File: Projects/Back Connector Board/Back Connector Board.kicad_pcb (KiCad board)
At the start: 2 copper layers, 12 parts, among them J1 Conn_02x09_Odd_Even, J10 Molex_MiniFit_02x04, J11 Molex_MiniFit_02x04, J12 Molex_MiniFit_02x04, J2 Conn_02x09_Odd_Even, J3 Conn_02x09_Odd_Even, J4 Conn_02x09_Odd_Even, J5 Conn_02x08_Odd_Even, J6 Conn_02x08_Odd_Even, J7 Molex_MiniFit_02x04, J8 Molex_MiniFit_02x04, J9 Molex_MiniFit_02x04

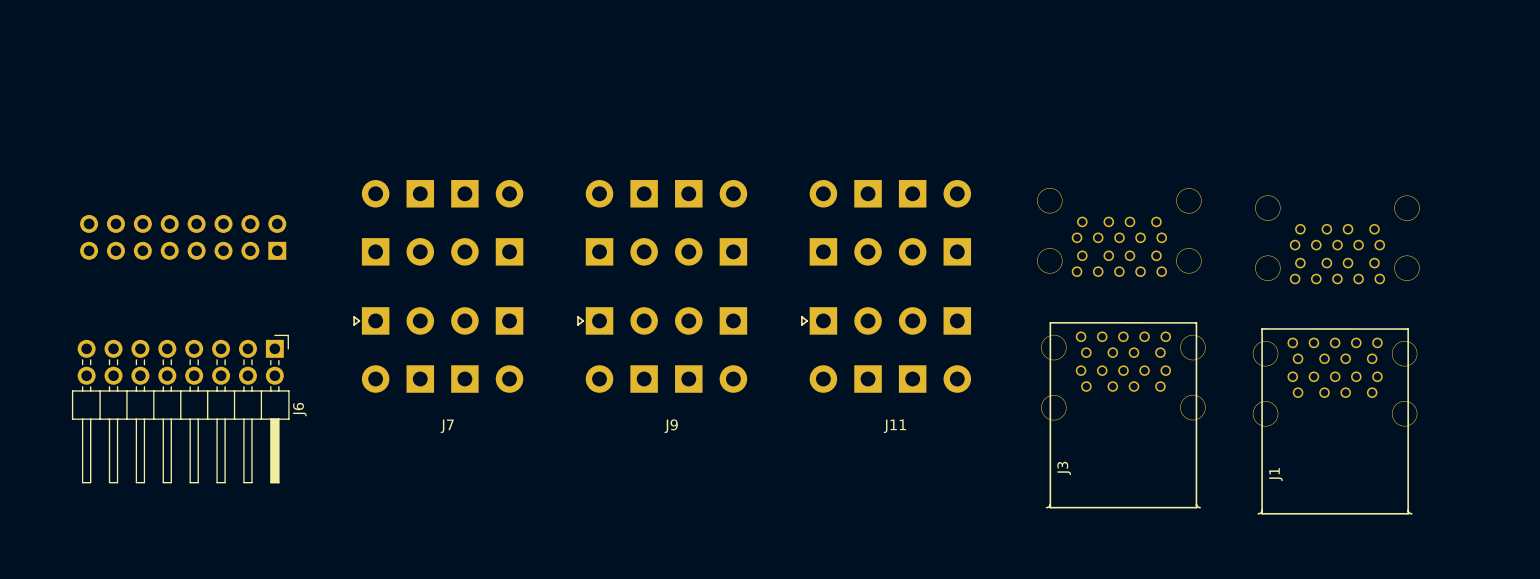
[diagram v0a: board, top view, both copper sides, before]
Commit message: Almost finished Back Connector Board; Just need to consult mechs
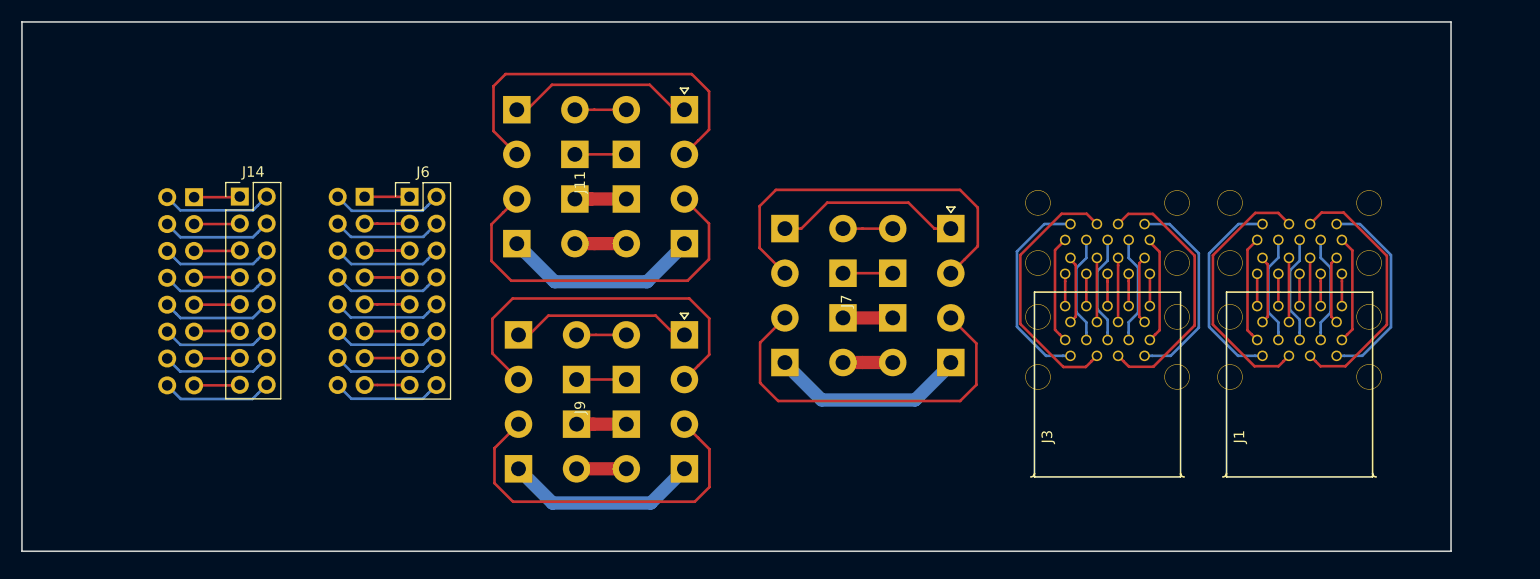
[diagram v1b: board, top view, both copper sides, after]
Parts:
- added J13: Conn_02x08_Odd_Even, Pin_Headers:Pin_Header_Straight_2x08_Pitch2.54mm, B.Cu at (107.5, 60.8)
- added J14: Conn_02x08_Odd_Even, Pin_Headers:Pin_Header_Straight_2x08_Pitch2.54mm, F.Cu at (111.9, 60.7)
- J5, J6: footprint Pin_Headers:Pin_Header_Angled_2x08_Pitch2.54mm -> Pin_Headers:Pin_Header_Straight_2x08_Pitch2.54mm
- moved J8 45.7 mm to (174.5, 70.6), turned to 270 degrees
- moved J11 39.4 mm to (142.7, 59.4), turned to 270 degrees
- moved J7 38.6 mm to (167.9, 70.6), turned to 270 degrees
- moved J10 26.0 mm to (149.3, 80.6), turned to 270 degrees
- moved J12 25.1 mm to (149.2, 59.4), turned to 270 degrees
- moved J6 19.2 mm to (127.9, 60.7), turned to 0 degrees
- moved J9 10.4 mm to (142.7, 80.6), turned to 270 degrees
- moved J5 9.70 mm to (123.6, 60.7), turned to 180 degrees
- moved J1 4.84 mm to (211.4, 73.3)
- moved J2 3.61 mm to (211.4, 65.8)
- moved J3 3.26 mm to (193.3, 73.3)
- moved J4 1.14 mm to (193.3, 65.8)
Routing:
- net Net-(J7-Pad2): track 0.00 -> 36.5 mm
- net Net-(J7-Pad3): track 0.00 -> 36.2 mm
- net Net-(J11-Pad2): track 0.00 -> 35.8 mm
- net Net-(J11-Pad3): track 0.00 -> 35.7 mm
- net Net-(J10-Pad2): track 0.00 -> 35.6 mm
- net Net-(J10-Pad3): track 0.00 -> 35.0 mm
- net Net-(J1-Pad3): track 0.00 -> 25.2 mm
- net Net-(J3-Pad3): track 0.00 -> 25.1 mm
- net Net-(J3-Pad2): track 0.00 -> 25.1 mm
- net Net-(J1-Pad2): track 0.00 -> 25.1 mm
- net Net-(J3-Pad4): track 0.00 -> 19.5 mm
- net Net-(J3-Pad1): track 0.00 -> 19.4 mm
- net Net-(J1-Pad4): track 0.00 -> 19.4 mm
- net Net-(J1-Pad1): track 0.00 -> 19.3 mm
- net Net-(J11-Pad4): track 0.00 -> 18.9 mm
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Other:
- board outline added: 135 x 50 mm

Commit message: Finished Back connector board to account for RPi cams
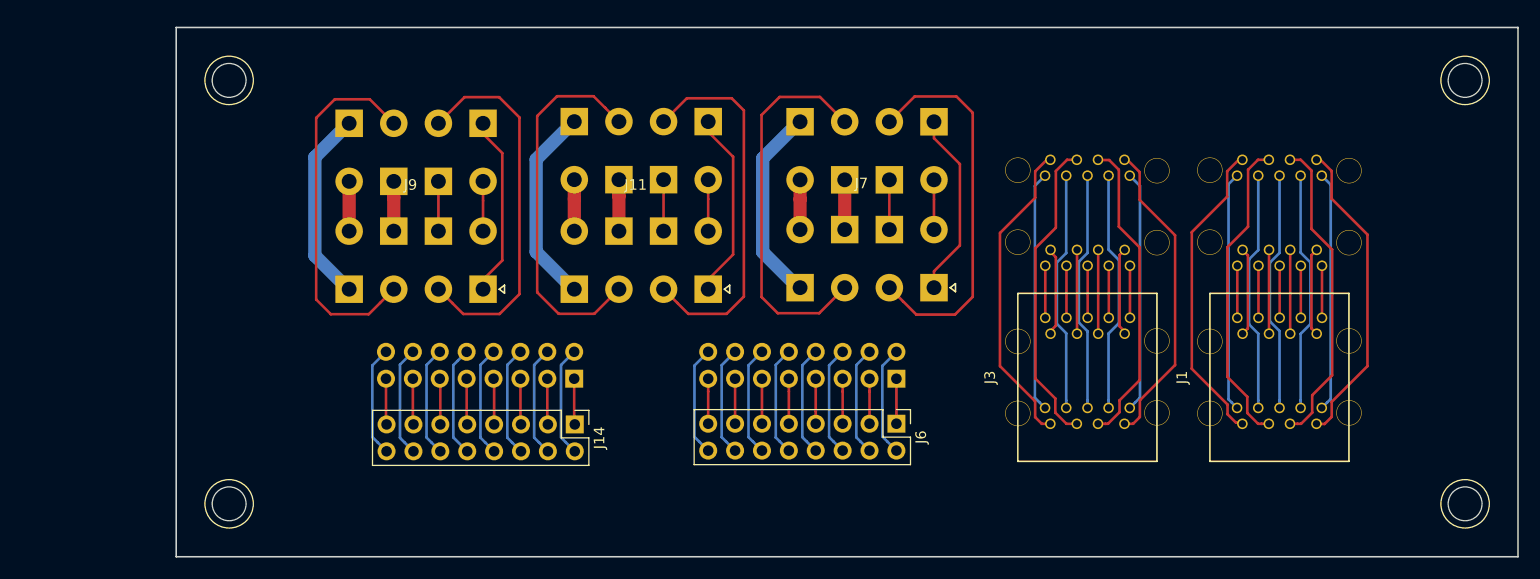
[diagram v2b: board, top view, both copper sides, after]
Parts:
- added REF**: 1pin, Connect:1pin, F.Cu at (227.6, 89.8)
- added REF**: 1pin, Connect:1pin, F.Cu at (227.6, 49.8)
- added REF**: 1pin, Connect:1pin, F.Cu at (110.8, 89.8)
- added REF**: 1pin, Connect:1pin, F.Cu at (110.8, 49.8)
- J1, J2, J3, J4: footprint USST-footprints:USB-A_3.0_Stacked_WM10420-ND -> USST-footprints:USBA_3.0_Stacked_Vertical-Molex_48409
- moved J5 53.1 mm to (173.9, 77.9), turned to 90 degrees
- moved J6 50.7 mm to (173.9, 82.2), turned to 270 degrees
- moved J13 39.8 mm to (143.4, 77.9), turned to 90 degrees
- moved J14 38.3 mm to (143.5, 82.2), turned to 270 degrees
- moved J9 26.7 mm to (128.0, 58.3), turned to 180 degrees
- moved J10 26.5 mm to (128.0, 64.9), turned to 180 degrees
- moved J7 12.7 mm to (170.6, 58.2), turned to 180 degrees
- moved J8 7.01 mm to (170.6, 64.8), turned to 180 degrees
- moved J11 6.60 mm to (149.2, 58.3), turned to 180 degrees
- moved J12 5.39 mm to (149.2, 64.8), turned to 180 degrees
- moved J1 4.73 mm to (210.1, 77.8)
- moved J3 4.73 mm to (191.9, 77.8)
- moved J2 4.39 mm to (210.1, 61.6)
- moved J4 4.39 mm to (191.9, 61.6)
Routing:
- net Net-(J3-Pad6): track 10.2 -> 22.8 mm
- net Net-(J3-Pad5): track 10.2 -> 22.7 mm
- net Net-(J1-Pad7): track 10.2 -> 22.7 mm
- net Net-(J3-Pad9): track 10.2 -> 22.7 mm
- net Net-(J1-Pad6): track 10.2 -> 22.7 mm
- net Net-(J3-Pad8): track 10.2 -> 22.7 mm
- net Net-(J1-Pad8): track 10.2 -> 22.7 mm
- net Net-(J1-Pad9): track 10.2 -> 22.6 mm
- net Net-(J1-Pad5): track 10.3 -> 22.6 mm
- net Net-(J3-Pad7): track 10.3 -> 22.6 mm
- net Net-(J3-Pad4): track 19.5 -> 29.8 mm
- net Net-(J1-Pad4): track 19.4 -> 29.6 mm
- net Net-(J3-Pad1): track 19.4 -> 29.6 mm
- net Net-(J1-Pad1): track 19.3 -> 29.4 mm
- net Net-(J1-Pad2): track 25.1 -> 29.4 mm
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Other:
- board size 135 x 50 mm -> 126.8 x 50 mm
